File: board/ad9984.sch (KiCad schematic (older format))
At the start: 39 parts, among them P401 AD9984 I2C, U401 AD9984

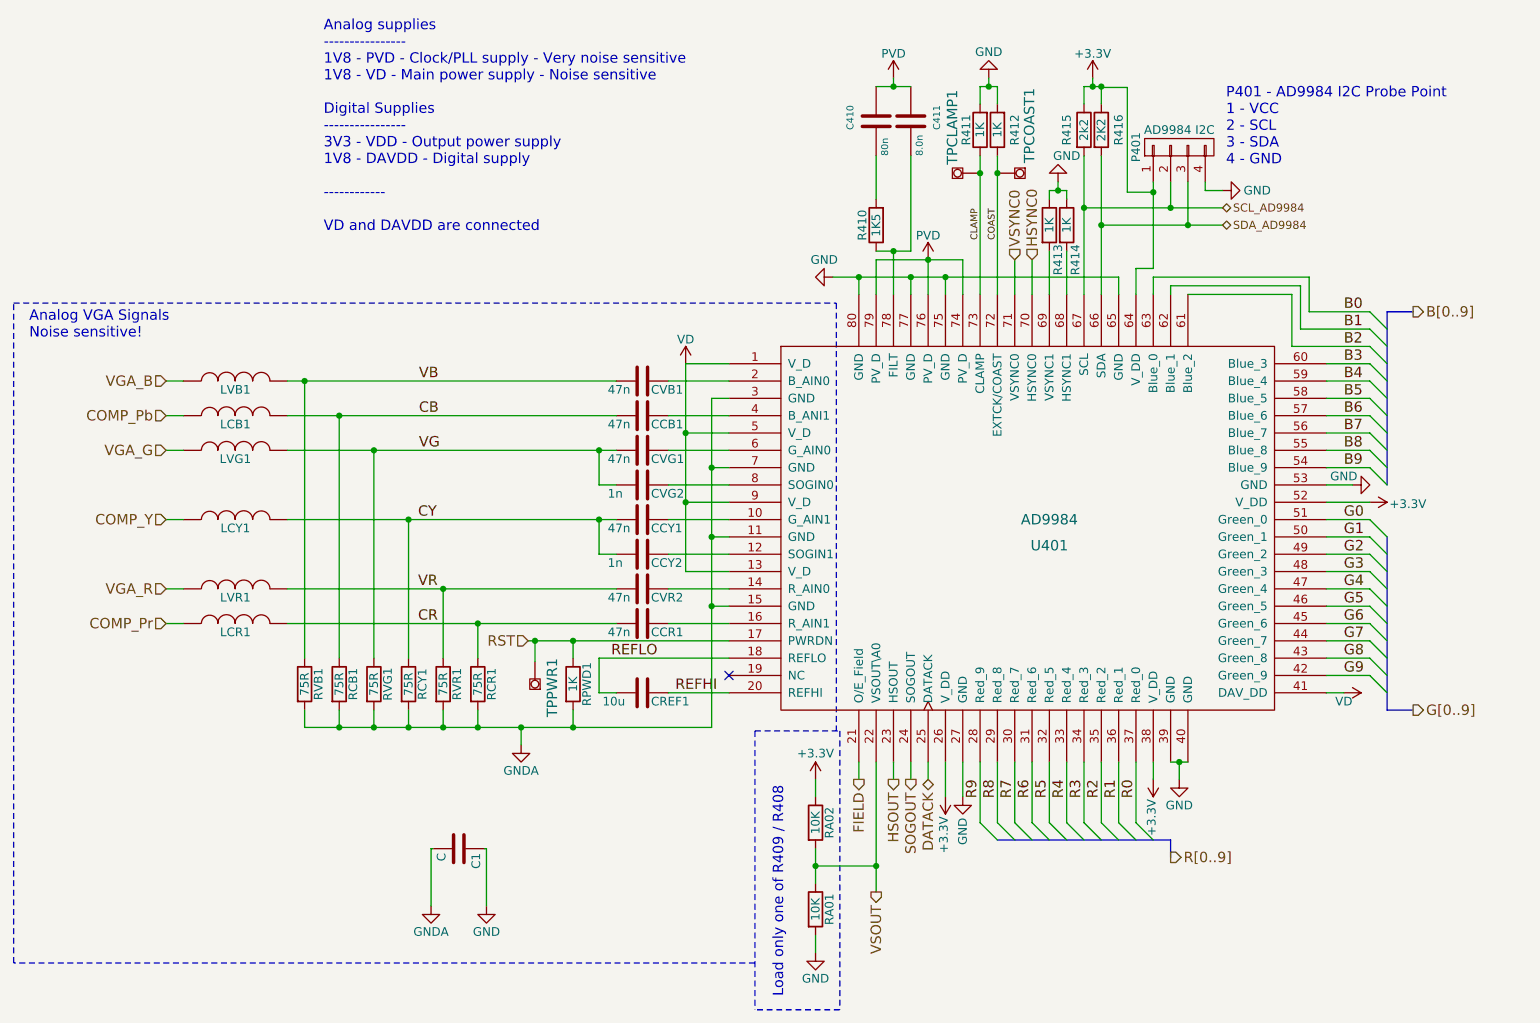
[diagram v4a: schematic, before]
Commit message: Updating net names.
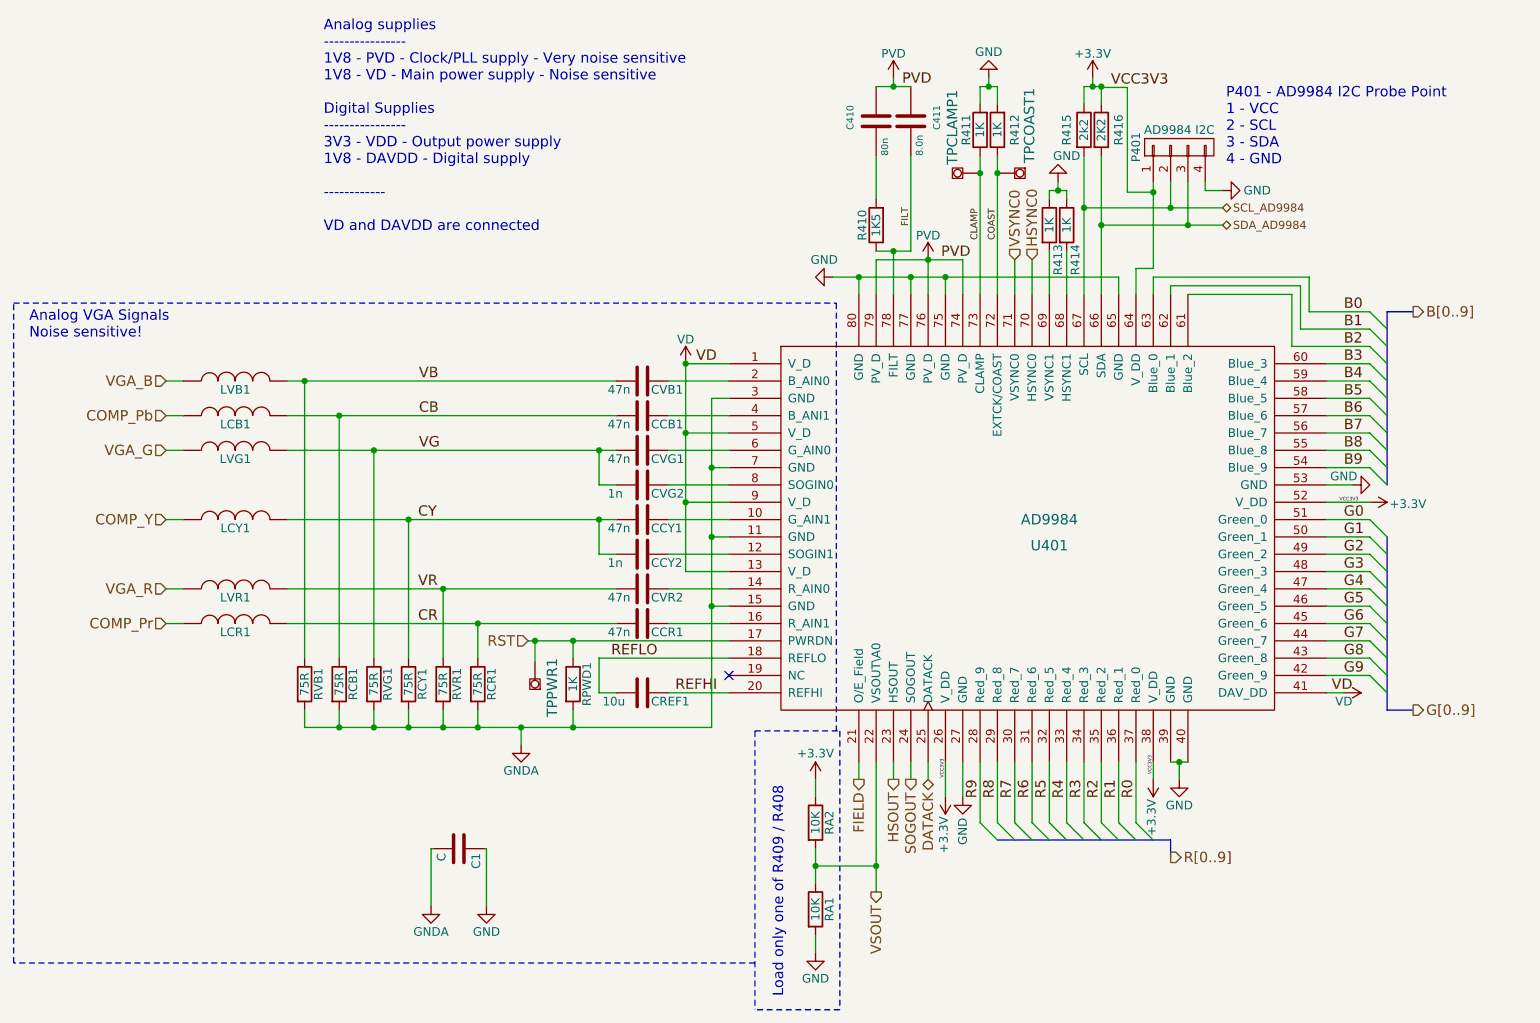
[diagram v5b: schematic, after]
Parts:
- renumbered RA01 to RA1, RA02 to RA2
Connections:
- net +3V3: now also P401.1 (P1), U401.64 (V_DD)
- net FILT: now reaches C411.2, R410.1, U401.78 (FILT)
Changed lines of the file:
@@
 R[0..9]
 $Comp
-L GNDA #PWR024
+L GNDA #PWR26
 U 1 1 5640DDDC
 P 4200 5050
-F 0 "#PWR024" H 4200 4800 50  0001 C CNN
+F 0 "#PWR26" H 4200 4800 50  0001 C CNN
 F 1 "GNDA" H 4200 4900 50  0000 C CNN
 F 2 "" H 4200 5050 60  0000 C CNN
@@
 VGA_R
 $Comp
-L +3.3V #PWR025
+L +3.3V #PWR38
 U 1 1 56413478
 P 7850 5250
-F 0 "#PWR025" H 7850 5100 50  0001 C CNN
+F 0 "#PWR38" H 7850 5100 50  0001 C CNN
 F 1 "+3.3V" V 7860 5470 50  0000 C CNN
 F 2 "" H 7850 5250 60  0000 C CNN
@@
 $EndComp
 $Comp
-L +3.3V #PWR026
+L +3.3V #PWR28
 U 1 1 56413584
 P 5900 5250
-F 0 "#PWR026" H 5900 5100 50  0001 C CNN
+F 0 "#PWR28" H 5900 5100 50  0001 C CNN
 F 1 "+3.3V" H 5900 5400 50  0000 C CNN
 F 2 "" H 5900 5250 60  0000 C CNN
@@
 $EndComp
 $Comp
-L VD #PWR027
+L VD #PWR27
 U 1 1 564135D1
 P 5150 2850
-F 0 "#PWR027" H 5150 2700 50  0001 C CNN
+F 0 "#PWR27" H 5150 2700 50  0001 C CNN
 F 1 "VD" H 5150 2990 50  0000 C CNN
 F 2 "" H 5150 2850 60  0000 C CNN
@@
 Connection ~ 4200 4950
 $Comp
-L R RA02
+L R RA2
 U 1 1 56414305
 P 5900 5500
-F 0 "RA02" V 5980 5500 50  0000 C CNN
+F 0 "RA2" V 5980 5500 50  0000 C CNN
 F 1 "10K" V 5900 5500 50  0000 C CNN
 F 2 "Resistors_SMD:R_0805_HandSoldering" V 5830 5500 30  0001 C CNN
@@
 $EndComp
 $Comp
-L R RA01
+L R RA1
 U 1 1 564143A0
 P 5900 6000
-F 0 "RA01" V 5980 6000 50  0000 C CNN
+F 0 "RA1" V 5980 6000 50  0000 C CNN
 F 1 "10K" V 5900 6000 50  0000 C CNN
 F 2 "Resistors_SMD:R_0805_HandSoldering" V 5830 6000 30  0001 C CNN
@@
 	5900 6150 5900 6250
 $Comp
-L GND #PWR028
+L GND #PWR29
 U 1 1 5641452A
 P 5900 6250
-F 0 "#PWR028" H 5900 6000 50  0001 C CNN
+F 0 "#PWR29" H 5900 6000 50  0001 C CNN
 F 1 "GND" H 5900 6100 50  0000 C CNN
 F 2 "" H 5900 6250 60  0000 C CNN
@@
 Connection ~ 3750 4950
 $Comp
-L GND #PWR029
+L GND #PWR34
 U 1 1 56415296
 P 6750 5350
-F 0 "#PWR029" H 6750 5100 50  0001 C CNN
+F 0 "#PWR34" H 6750 5100 50  0001 C CNN
 F 1 "GND" V 6750 5150 50  0000 C CNN
 F 2 "" H 6750 5350 60  0000 C CNN
@@
 $EndComp
 $Comp
-L GND #PWR030
+L GND #PWR39
 U 1 1 5641579B
 P 8000 5250
-F 0 "#PWR030" H 8000 5000 50  0001 C CNN
+F 0 "#PWR39" H 8000 5000 50  0001 C CNN
 F 1 "GND" H 8000 5100 50  0000 C CNN
 F 2 "" H 8000 5250 60  0000 C CNN
@@
 DATACK
 $Comp
-L PVD #PWR031
+L PVD #PWR32
 U 1 1 56415C22
 P 6550 2250
-F 0 "#PWR031" H 6550 2100 50  0001 C CNN
+F 0 "#PWR32" H 6550 2100 50  0001 C CNN
 F 1 "PVD" H 6550 2390 50  0000 C CNN
 F 2 "" H 6550 2250 60  0000 C CNN
@@
 	7150 2450 7150 2250
 $Comp
-L GND #PWR032
+L GND #PWR30
 U 1 1 564164E1
 P 6000 2350
-F 0 "#PWR032" H 6000 2100 50  0001 C CNN
+F 0 "#PWR30" H 6000 2100 50  0001 C CNN
 F 1 "GND" V 5900 2300 50  0000 C CNN
 F 2 "" H 6000 2350 60  0000 C CNN
@@
 Connection ~ 6150 2350
 $Comp
-L VD #PWR033
+L VD #PWR41
 U 1 1 56416F9D
 P 8950 4750
-F 0 "#PWR033" H 8950 4600 50  0001 C CNN
+F 0 "#PWR41" H 8950 4600 50  0001 C CNN
 F 1 "VD" V 9000 4750 50  0000 C CNN
 F 2 "" H 8950 4750 60  0000 C CNN
@@
 $EndComp
 $Comp
-L GND #PWR034
+L GND #PWR42
 U 1 1 564170A0
 P 9000 3550
-F 0 "#PWR034" H 9000 3300 50  0001 C CNN
+F 0 "#PWR42" H 9000 3300 50  0001 C CNN
 F 1 "GND" V 9050 3600 50  0000 C CNN
 F 2 "" H 9000 3550 60  0000 C CNN
@@
 $EndComp
 $Comp
-L GND #PWR035
+L GND #PWR35
 U 1 1 564172D9
 P 6900 1200
-F 0 "#PWR035" H 6900 950 50  0001 C CNN
+F 0 "#PWR35" H 6900 950 50  0001 C CNN
 F 1 "GND" H 6900 1050 50  0000 C CNN
 F 2 "" H 6900 1200 60  0000 C CNN
@@
 $EndComp
 $Comp
-L PVD #PWR036
+L PVD #PWR31
 U 1 1 56417326
 P 6350 1200
-F 0 "#PWR036" H 6350 1050 50  0001 C CNN
+F 0 "#PWR31" H 6350 1050 50  0001 C CNN
 F 1 "PVD" H 6350 1340 50  0000 C CNN
 F 2 "" H 6350 1200 60  0000 C CNN
@@
 $EndComp
 $Comp
-L GND #PWR037
+L GND #PWR36
 U 1 1 5655A202
 P 7300 1800
-F 0 "#PWR037" H 7300 1550 50  0001 C CNN
+F 0 "#PWR36" H 7300 1550 50  0001 C CNN
 F 1 "GND" H 7250 1650 50  0000 C CNN
 F 2 "" H 7300 1800 60  0000 C CNN
@@
 $EndComp
 $Comp
-L GND #PWR038
+L GND #PWR40
 U 1 1 5692FBEE
 P 8250 1850
-F 0 "#PWR038" H 8250 1600 50  0001 C CNN
+F 0 "#PWR40" H 8250 1600 50  0001 C CNN
 F 1 "GND" V 8250 1650 50  0000 C CNN
 F 2 "" H 8250 1850 50  0000 C CNN
@@
 Connection ~ 8050 2050
 $Comp
-L GNDA #PWR039
+L GNDA #PWR24
 U 1 1 57976F35
 P 3680 5980
-F 0 "#PWR039" H 3680 5730 50  0001 C CNN
+F 0 "#PWR24" H 3680 5730 50  0001 C CNN
 F 1 "GNDA" H 3680 5830 50  0000 C CNN
 F 2 "" H 3680 5980 60  0000 C CNN
@@
 $EndComp
 $Comp
-L GND #PWR040
+L GND #PWR25
 U 1 1 57976FB5
 P 4000 5980
-F 0 "#PWR040" H 4000 5730 50  0001 C CNN
+F 0 "#PWR25" H 4000 5730 50  0001 C CNN
 F 1 "GND" H 4000 5830 50  0000 C CNN
 F 2 "" H 4000 5980 60  0000 C CNN
@@
 	4000 5980 4000 5650
 $Comp
-L +3.3V #PWR041
+L +3.3V #PWR37
 U 1 1 5796E857
 P 7500 1200
-F 0 "#PWR041" H 7500 1050 50  0001 C CNN
+F 0 "#PWR37" H 7500 1050 50  0001 C CNN
 F 1 "+3.3V" H 7500 1340 50  0000 C CNN
 F 2 "" H 7500 1200 50  0000 C CNN
@@
 Connection ~ 7550 1250
 $Comp
-L +3.3V #PWR042
+L +3.3V #PWR33
 U 1 1 5796EFF3
 P 6650 5350
-F 0 "#PWR042" H 6650 5200 50  0001 C CNN
+F 0 "#PWR33" H 6650 5200 50  0001 C CNN
 F 1 "+3.3V" V 6660 5570 50  0000 C CNN
 F 2 "" H 6650 5350 60  0000 C CNN
@@
 $EndComp
 $Comp
-L +3.3V #PWR043
+L +3.3V #PWR43
 U 1 1 5796F1FD
 P 9100 3650
-F 0 "#PWR043" H 9100 3500 50  0001 C CNN
+F 0 "#PWR43" H 9100 3500 50  0001 C CNN
 F 1 "+3.3V" V 9110 3870 50  0000 C CNN
 F 2 "" H 9100 3650 60  0000 C CNN
@@
 Text Label 6950 2135 1    39   ~ 0
 COAST
+Text Label 7605 1255 0    60   ~ 0
+VCC3V3
+Text Label 6400 1250 0    60   ~ 0
+PVD
+Text Label 6625 2250 0    60   ~ 0
+PVD
+Text Label 8880 4750 0    60   ~ 0
+VD
+Text Label 7850 5220 1    20   ~ 0
+VCC3V3
+Text Label 6650 5240 1    20   ~ 0
+VCC3V3
+Text Label 5210 2850 0    60   ~ 0
+VD
+Connection ~ 5150 2850
+Text Label 9035 3650 2    20   ~ 0
+VCC3V3
+Text Label 6450 2055 1    39   ~ 0
+FILT
 $EndSCHEMATC

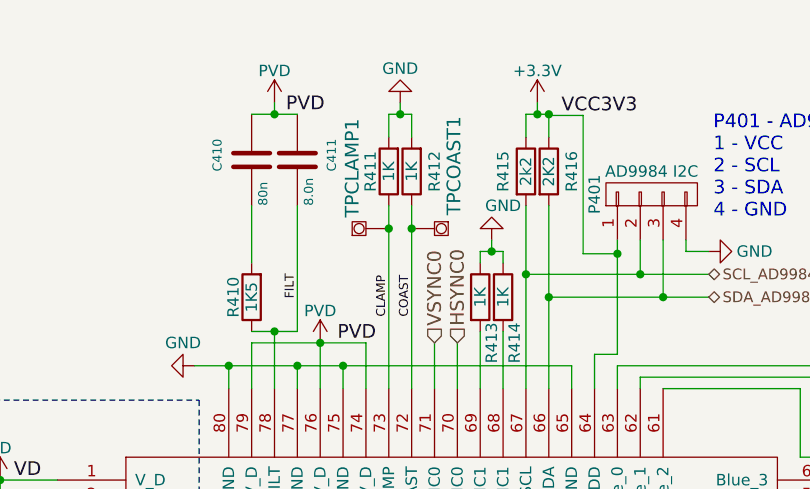
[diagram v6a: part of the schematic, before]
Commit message: ERC and removing 0 from vsync/hsync.
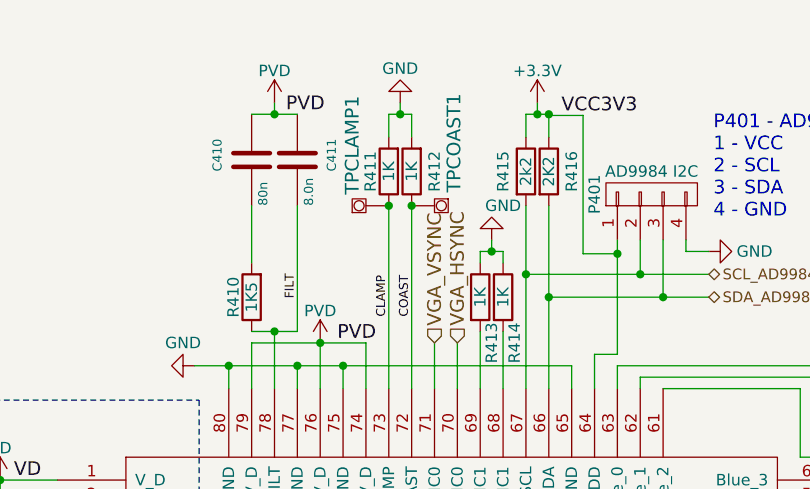
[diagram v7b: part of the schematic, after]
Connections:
- net HSYNC0 renamed VGA_HSYNC
- net VSYNC0 renamed VGA_VSYNC
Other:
- moved on the sheet: TPCLAMP1, TPCOAST1
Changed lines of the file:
@@
 $EndComp
 Text HLabel 7050 2250 1    60   Input ~ 0
-VSYNC0
+VGA_VSYNC
 Text HLabel 7150 2250 1    60   Input ~ 0
-HSYNC0
+VGA_HSYNC
 $Comp
 L R R415
@@
 Connection ~ 6900 1250
 Wire Wire Line
+	6850 1650 6850 1650
+Wire Wire Line
 	6850 1650 6850 2450
+Wire Wire Line
+	6950 1650 6950 1650
 Wire Wire Line
 	6950 1650 6950 2450
@@
 L TESTPOINT TPCOAST1
 U 1 1 56463E75
-P 6950 1750
-F 0 "TPCOAST1" H 6675 1935 60  0000 C CNN
-F 1 "TESTPOINT" H 6950 1700 60  0001 C CNN
-F 2 "2MM-TESTPOINT:2MM-TESTPOINT" H 6950 1750 60  0001 C CNN
-F 3 "" H 6950 1750 60  0000 C CNN
-	1    6950 1750
+P 6950 1650
+F 0 "TPCOAST1" H 6675 1835 60  0000 C CNN
+F 1 "TESTPOINT" H 6950 1600 60  0001 C CNN
+F 2 "2MM-TESTPOINT:2MM-TESTPOINT" H 6950 1650 60  0001 C CNN
+F 3 "" H 6950 1650 60  0000 C CNN
+	1    6950 1650
 	0    1    1    0
 $EndComp
@@
 L TESTPOINT TPCLAMP1
 U 1 1 56463EBE
-P 6850 1750
-F 0 "TPCLAMP1" H 7115 1910 60  0000 C CNN
-F 1 "TESTPOINT" H 6850 1700 60  0001 C CNN
-F 2 "2MM-TESTPOINT:2MM-TESTPOINT" H 6850 1750 60  0001 C CNN
-F 3 "" H 6850 1750 60  0000 C CNN
-	1    6850 1750
+P 6850 1650
+F 0 "TPCLAMP1" H 7115 1810 60  0000 C CNN
+F 1 "TESTPOINT" H 6850 1600 60  0001 C CNN
+F 2 "2MM-TESTPOINT:2MM-TESTPOINT" H 6850 1650 60  0001 C CNN
+F 3 "" H 6850 1650 60  0000 C CNN
+	1    6850 1650
 	0    -1   -1   0
 $EndComp
-Connection ~ 6850 1750
-Connection ~ 6950 1750
+Connection ~ 6850 1650
+Connection ~ 6950 1650
 $Comp
 L R R413

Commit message: Giving things better names.
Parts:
- renumbered P401 to PAD_I2C0, U401 to UAD9984
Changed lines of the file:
@@
 $EndDescr
 $Comp
-L AD9984 U401
+L AD9984 UAD9984
 U 1 1 53727604
 P 7150 3800
-F 0 "U401" H 7250 3700 60  0000 C CNN
+F 0 "UAD9984" H 7250 3700 60  0000 C CNN
 F 1 "AD9984" H 7250 3850 60  0000 C CNN
 F 2 "analog-devices2:analog-devices2-LQFP80" H 6350 4050 60  0001 C CNN
@@
 Connection ~ 4500 4950
 $Comp
-L CONN_01X04 P401
+L CONN_01X04 PAD_I2C0
 U 1 1 5692F854
 P 8000 1600
-F 0 "P401" H 8000 1850 50  0000 C CNN
+F 0 "PAD_I2C0" H 8000 1850 50  0000 C CNN
 F 1 "AD9984 I2C" V 8100 1600 50  0000 C CNN
 F 2 "CON-SMD-2.54:HARWIN-M20-87-4x1" H 8000 1600 50  0001 C CNN
